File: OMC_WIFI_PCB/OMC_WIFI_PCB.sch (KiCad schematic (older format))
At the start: 14 parts, among them J1 ESP32_Left, J10 Control_ACS712, J11 Control_ZMPT101B, J2 ESP32_Right, J3 Power_In, J4 Switch, J5 Pins_FT232R, J6 Line_Relay, J7 Control_Relay, J8 Line_ACS712, J9 Line_ZMPT101B

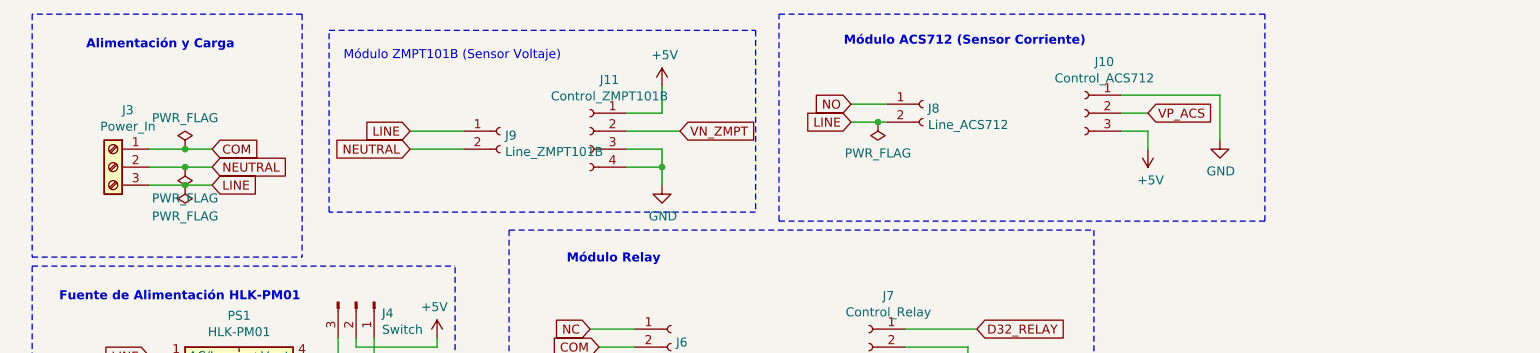
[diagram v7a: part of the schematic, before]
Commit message: Actualización PCB
+ Jumper para ACS
+ Fusible
> Rediseño de la PCB
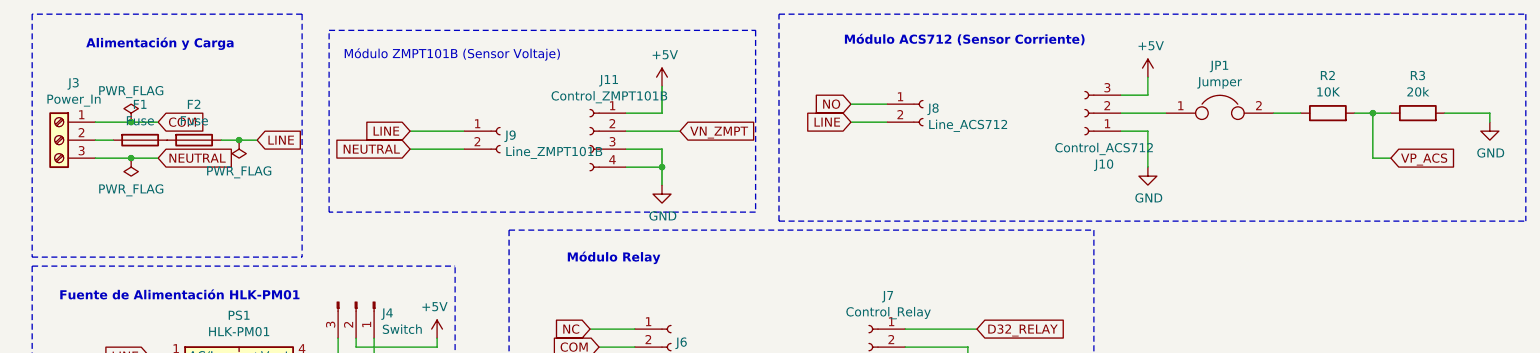
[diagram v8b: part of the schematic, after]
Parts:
- added F1, F2: Fuse, Fuse:Fuse_Littelfuse_395Series, symbol Device:Fuse
- added JP1: Jumper, Connector_PinHeader_1.00mm:PinHeader_1x02_P1.00mm_Vertical, symbol Device:Jumper
- added R2: 10K, Resistor_SMD:R_2010_5025Metric_Pad1.40x2.65mm_HandSolder, symbol Device:R
- added R3: 20k, Resistor_SMD:R_2010_5025Metric_Pad1.40x2.65mm_HandSolder, symbol Device:R
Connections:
- net GND: now also R3.2
- net LINE: now also F2.1; no longer J3.3 (Pin_3)
- net NEUTRAL: now also J3.3 (Pin_3); no longer J3.2 (Pin_2)
- net VP_ACS: now also R2.2, R3.1; no longer J10.2 (Pin_2)
- new net: J10.2 (Pin_2), JP1.1
- new net: F1.1, F2.2
- new net: F1.2, J3.2 (Pin_2)
- new net: JP1.2, R2.1
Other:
- moved on the sheet: J3
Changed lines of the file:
@@
 L power:PWR_FLAG #FLG0101
 U 1 1 622CF9F0
-P 1550 1350
-F 0 "#FLG0101" H 1550 1425 50  0001 C CNN
-F 1 "PWR_FLAG" H 1550 1523 50  0000 C CNN
-F 2 "" H 1550 1350 50  0001 C CNN
-F 3 "~" H 1550 1350 50  0001 C CNN
-	1    1550 1350
+P 1250 1200
+F 0 "#FLG0101" H 1250 1275 50  0001 C CNN
+F 1 "PWR_FLAG" H 1250 1373 50  0000 C CNN
+F 2 "" H 1250 1200 50  0001 C CNN
+F 3 "~" H 1250 1200 50  0001 C CNN
+	1    1250 1200
 	1    0    0    -1
 $EndComp
@@
 L Connector:Screw_Terminal_01x03 J3
 U 1 1 6243119F
-P 1150 1450
-F 0 "J3" H 1068 1767 50  0000 C CNN
-F 1 "Power_In" H 1068 1676 50  0000 C CNN
-F 2 "6PCV-03-006:TE_5-1437652-4" H 1150 1450 50  0001 C CNN
-F 3 "~" H 1150 1450 50  0001 C CNN
-	1    1150 1450
+P 850 1300
+F 0 "J3" H 768 1617 50  0000 C CNN
+F 1 "Power_In" H 768 1526 50  0000 C CNN
+F 2 "6PCV-03-006:TE_5-1437652-4" H 850 1300 50  0001 C CNN
+F 3 "~" H 850 1300 50  0001 C CNN
+	1    850  1300
 	-1   0    0    -1
 $EndComp
@@
 	3800 2350 4050 2350
 Wire Wire Line
-	5700 2550 5700 2600
-Wire Wire Line
-	5550 2550 5700 2550
-Wire Wire Line
 	5900 2450 5900 2750
 Wire Wire Line
@@
 NoConn ~ 3800 2900
 Wire Wire Line
-	1350 1350 1550 1350
-Text GLabel 1350 2500 0    50   Input ~ 0
-LINE
-Text GLabel 1350 2700 0    50   Input ~ 0
-NEUTRAL
+	1050 1200 1250 1200
 Wire Wire Line
 	1450 2700 1350 2700
@@
 Wire Notes Line
 	6050 3250 600  3250
-Text GLabel 2800 1350 0    50   Input ~ 0
-NEUTRAL
-Wire Notes Line
-	7550 1750 7550 600
 Wire Notes Line
 	4850 1750 4850 600
-Wire Notes Line
-	4850 1750 7550 1750
-Wire Wire Line
-	6750 1150 6900 1150
-Wire Wire Line
-	7300 1050 7300 1300
-Wire Wire Line
-	6750 1050 7300 1050
-Wire Wire Line
-	6900 1250 6900 1350
-Wire Wire Line
-	6750 1250 6900 1250
+Wire Wire Line
+	6900 1050 6900 950
+Wire Wire Line
+	6750 1050 6900 1050
 $Comp
 L power:GND #PWR0110
 U 1 1 620E6BF1
-P 7300 1300
-F 0 "#PWR0110" H 7300 1050 50  0001 C CNN
-F 1 "GND" H 7305 1127 50  0000 C CNN
-F 2 "" H 7300 1300 50  0001 C CNN
-F 3 "" H 7300 1300 50  0001 C CNN
-	1    7300 1300
+P 6900 1450
+F 0 "#PWR0110" H 6900 1200 50  0001 C CNN
+F 1 "GND" H 6905 1277 50  0000 C CNN
+F 2 "" H 6900 1450 50  0001 C CNN
+F 3 "" H 6900 1450 50  0001 C CNN
+	1    6900 1450
 	1    0    0    -1
 $EndComp
@@
 L power:+5V #PWR0109
 U 1 1 620E6405
-P 6900 1350
-F 0 "#PWR0109" H 6900 1200 50  0001 C CNN
-F 1 "+5V" H 6915 1523 50  0000 C CNN
-F 2 "" H 6900 1350 50  0001 C CNN
-F 3 "" H 6900 1350 50  0001 C CNN
-	1    6900 1350
-	1    0    0    1
-$EndComp
-Text GLabel 6900 1150 2    50   Input ~ 0
+P 6900 950
+F 0 "#PWR0109" H 6900 800 50  0001 C CNN
+F 1 "+5V" H 6915 1123 50  0000 C CNN
+F 2 "" H 6900 950 50  0001 C CNN
+F 3 "" H 6900 950 50  0001 C CNN
+	1    6900 950
+	1    0    0    -1
+$EndComp
+Text GLabel 8250 1400 2    50   Input ~ 0
 VP_ACS
 $Comp
@@
 F 3 "~" H 6550 1150 50  0001 C CNN
 	1    6550 1150
-	-1   0    0    -1
-$EndComp
-Wire Notes Line
-	4850 600  7550 600
+	-1   0    0    1
+$EndComp
 Wire Wire Line
 	4000 1250 4300 1250
@@
 	2350 690  4720 690
 Wire Notes Line
-	2200 600  2200 1950
-Wire Notes Line
 	700  600  700  1950
-Connection ~ 5400 1200
-$Comp
-L power:PWR_FLAG #FLG0105
-U 1 1 624FAE80
-P 5400 1200
-F 0 "#FLG0105" H 5400 1275 50  0001 C CNN
-F 1 "PWR_FLAG" H 5400 1373 50  0000 C CNN
-F 2 "" H 5400 1200 50  0001 C CNN
-F 3 "~" H 5400 1200 50  0001 C CNN
-	1    5400 1200
-	1    0    0    1
-$EndComp
-Text GLabel 5250 1200 0    50   Input ~ 0
-LINE
-Wire Wire Line
-	5250 1200 5400 1200
-Wire Wire Line
-	5400 1200 5450 1200
 Wire Wire Line
 	5250 1100 5450 1100
-$Comp
-L Connector:Conn_01x02_Female J8
-U 1 1 621188AB
-P 5650 1100
-F 0 "J8" H 5678 1076 50  0000 L CNN
-F 1 "Line_ACS712" H 5678 985 50  0000 L CNN
-F 2 "TerminalBlock:TerminalBlock_bornier-2_P5.08mm" H 5650 1100 50  0001 C CNN
-F 3 "~" H 5650 1100 50  0001 C CNN
-	1    5650 1100
-	1    0    0    -1
-$EndComp
 Wire Wire Line
 	3100 1350 2800 1350
@@
 D27
 NoConn ~ 1950 6700
-Text GLabel 1700 1350 2    50   Input ~ 0
-COM
-Wire Wire Line
-	1700 1350 1550 1350
-Connection ~ 1550 1350
-Wire Wire Line
-	1700 1550 1550 1550
-Wire Wire Line
-	1700 1450 1550 1450
-Wire Wire Line
-	1550 1450 1350 1450
-Connection ~ 1550 1450
-$Comp
-L power:PWR_FLAG #FLG0102
-U 1 1 622D0110
-P 1550 1450
-F 0 "#FLG0102" H 1550 1525 50  0001 C CNN
-F 1 "PWR_FLAG" H 1550 1623 50  0000 C CNN
-F 2 "" H 1550 1450 50  0001 C CNN
-F 3 "~" H 1550 1450 50  0001 C CNN
-	1    1550 1450
-	1    0    0    1
-$EndComp
-$Comp
-L power:PWR_FLAG #FLG0103
-U 1 1 62127B9A
-P 1550 1550
-F 0 "#FLG0103" H 1550 1625 50  0001 C CNN
-F 1 "PWR_FLAG" H 1550 1723 50  0000 C CNN
-F 2 "" H 1550 1550 50  0001 C CNN
-F 3 "~" H 1550 1550 50  0001 C CNN
-	1    1550 1550
-	1    0    0    1
-$EndComp
-Connection ~ 1550 1550
-Wire Wire Line
-	1550 1550 1350 1550
+Wire Wire Line
+	1400 1200 1250 1200
+Connection ~ 1250 1200
 Wire Notes Line
 	700  1950 2200 1950
@@
 	2400 2400 2400 2700
 Connection ~ 2400 2700
+Wire Wire Line
+	2600 2400 2600 2500
+Wire Wire Line
+	2600 2500 2250 2500
+Wire Wire Line
+	2500 2400 2500 2450
+Wire Wire Line
+	2500 2450 2950 2450
+Wire Wire Line
+	2950 2450 2950 2400
+Wire Wire Line
+	5550 2550 5700 2550
+Wire Wire Line
+	5700 2550 5700 2600
+$Comp
+L Connector:Conn_01x02_Female J8
+U 1 1 621188AB
+P 5650 1100
+F 0 "J8" H 5678 1076 50  0000 L CNN
+F 1 "Line_ACS712" H 5678 985 50  0000 L CNN
+F 2 "TerminalBlock:TerminalBlock_bornier-2_P5.08mm" H 5650 1100 50  0001 C CNN
+F 3 "~" H 5650 1100 50  0001 C CNN
+	1    5650 1100
+	1    0    0    -1
+$EndComp
+Wire Wire Line
+	5250 1200 5450 1200
+Wire Notes Line
+	2200 600  2200 1950
+Text GLabel 1400 1200 2    50   Input ~ 0
+COM
+Text GLabel 1350 2700 0    50   Input ~ 0
+NEUTRAL
+Text GLabel 1350 2500 0    50   Input ~ 0
+LINE
+Text GLabel 5250 1200 0    50   Input ~ 0
+LINE
+Text GLabel 2800 1350 0    50   Input ~ 0
+NEUTRAL
 Text GLabel 2800 1250 0    50   Input ~ 0
 LINE
-Text GLabel 1700 1550 2    50   Input ~ 0
+Wire Wire Line
+	1400 1400 1250 1400
+$Comp
+L power:PWR_FLAG #FLG0102
+U 1 1 622D0110
+P 1250 1400
+F 0 "#FLG0102" H 1250 1475 50  0001 C CNN
+F 1 "PWR_FLAG" H 1250 1573 50  0000 C CNN
+F 2 "" H 1250 1400 50  0001 C CNN
+F 3 "~" H 1250 1400 50  0001 C CNN
+	1    1250 1400
+	1    0    0    1
+$EndComp
+Text GLabel 1400 1400 2    50   Input ~ 0
+NEUTRAL
+$Comp
+L power:PWR_FLAG #FLG0103
+U 1 1 62127B9A
+P 1850 1300
+F 0 "#FLG0103" H 1850 1375 50  0001 C CNN
+F 1 "PWR_FLAG" H 1850 1473 50  0000 C CNN
+F 2 "" H 1850 1300 50  0001 C CNN
+F 3 "~" H 1850 1300 50  0001 C CNN
+	1    1850 1300
+	1    0    0    1
+$EndComp
+Wire Wire Line
+	1950 1300 1850 1300
+Wire Wire Line
+	1750 1300 1850 1300
+Connection ~ 1850 1300
+$Comp
+L Device:Fuse F1
+U 1 1 6211FE5D
+P 1300 1300
+F 0 "F1" V 1103 1300 50  0000 C CNN
+F 1 "Fuse" V 1194 1300 50  0000 C CNN
+F 2 "Fuse:Fuse_Littelfuse_395Series" V 1230 1300 50  0001 C CNN
+F 3 "~" H 1300 1300 50  0001 C CNN
+	1    1300 1300
+	0    1    1    0
+$EndComp
+$Comp
+L Device:Fuse F2
+U 1 1 6214DC3E
+P 1600 1300
+F 0 "F2" V 1403 1300 50  0000 C CNN
+F 1 "Fuse" V 1494 1300 50  0000 C CNN
+F 2 "Fuse:Fuse_Littelfuse_395Series" V 1530 1300 50  0001 C CNN
+F 3 "~" H 1600 1300 50  0001 C CNN
+	1    1600 1300
+	0    1    1    0
+$EndComp
+Text GLabel 1950 1300 2    50   Input ~ 0
 LINE
-Text GLabel 1700 1450 2    50   Input ~ 0
-NEUTRAL
-Wire Wire Line
-	2600 2400 2600 2500
-Wire Wire Line
-	2600 2500 2250 2500
-Wire Wire Line
-	2500 2400 2500 2450
-Wire Wire Line
-	2500 2450 2950 2450
-Wire Wire Line
-	2950 2450 2950 2400
+Wire Wire Line
+	1050 1300 1150 1300
+Wire Wire Line
+	1050 1400 1250 1400
+Connection ~ 1250 1400
+Wire Wire Line
+	6750 1250 6900 1250
+Wire Wire Line
+	6900 1250 6900 1450
+$Comp
+L Device:Jumper JP1
+U 1 1 621BDC2F
+P 7300 1150
+F 0 "JP1" H 7300 1414 50  0000 C CNN
+F 1 "Jumper" H 7300 1323 50  0000 C CNN
+F 2 "Connector_PinHeader_1.00mm:PinHeader_1x02_P1.00mm_Vertical" H 7300 1150 50  0001 C CNN
+F 3 "~" H 7300 1150 50  0001 C CNN
+	1    7300 1150
+	1    0    0    -1
+$EndComp
+Wire Wire Line
+	6750 1150 7000 1150
+$Comp
+L Device:R R2
+U 1 1 621CBE6C
+P 7900 1150
+F 0 "R2" V 8107 1150 50  0000 C CNN
+F 1 "10K" V 8016 1150 50  0000 C CNN
+F 2 "Resistor_SMD:R_2010_5025Metric_Pad1.40x2.65mm_HandSolder" V 7830 1150 50  0001 C CNN
+F 3 "~" H 7900 1150 50  0001 C CNN
+	1    7900 1150
+	0    -1   -1   0
+$EndComp
+$Comp
+L Device:R R3
+U 1 1 621CF98B
+P 8400 1150
+F 0 "R3" V 8607 1150 50  0000 C CNN
+F 1 "20k" V 8516 1150 50  0000 C CNN
+F 2 "Resistor_SMD:R_2010_5025Metric_Pad1.40x2.65mm_HandSolder" V 8330 1150 50  0001 C CNN
+F 3 "~" H 8400 1150 50  0001 C CNN
+	1    8400 1150
+	0    -1   -1   0
+$EndComp
+$Comp
+L power:GND #PWR0111
+U 1 1 621D76EE
+P 8800 1200
+F 0 "#PWR0111" H 8800 950 50  0001 C CNN
+F 1 "GND" H 8805 1027 50  0000 C CNN
+F 2 "" H 8800 1200 50  0001 C CNN
+F 3 "" H 8800 1200 50  0001 C CNN
+	1    8800 1200
+	1    0    0    -1
+$EndComp
+Wire Wire Line
+	7600 1150 7750 1150
+Wire Wire Line
+	8050 1150 8150 1150
+Wire Wire Line
+	8550 1150 8800 1150
+Wire Wire Line
+	8800 1150 8800 1200
+Wire Wire Line
+	8250 1400 8150 1400
+Wire Wire Line
+	8150 1400 8150 1150
+Connection ~ 8150 1150
+Wire Wire Line
+	8150 1150 8250 1150
+Wire Notes Line
+	4850 600  9000 600
+Wire Notes Line
+	4850 1750 9000 1750
+Wire Notes Line
+	9000 600  9000 1750
 $EndSCHEMATC
